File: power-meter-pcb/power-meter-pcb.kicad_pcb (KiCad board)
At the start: 4 copper layers, 23 x 51.5 mm, 62 parts, among them J1 Crank interconnect, J2 Debug, J3 Spare GPIO pins, J4 Battery, J5 USB4120-03-C_REVA, J6 Side A, J7 Side B, Q1 AS2302, SW1 EN, SW2 BOOT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

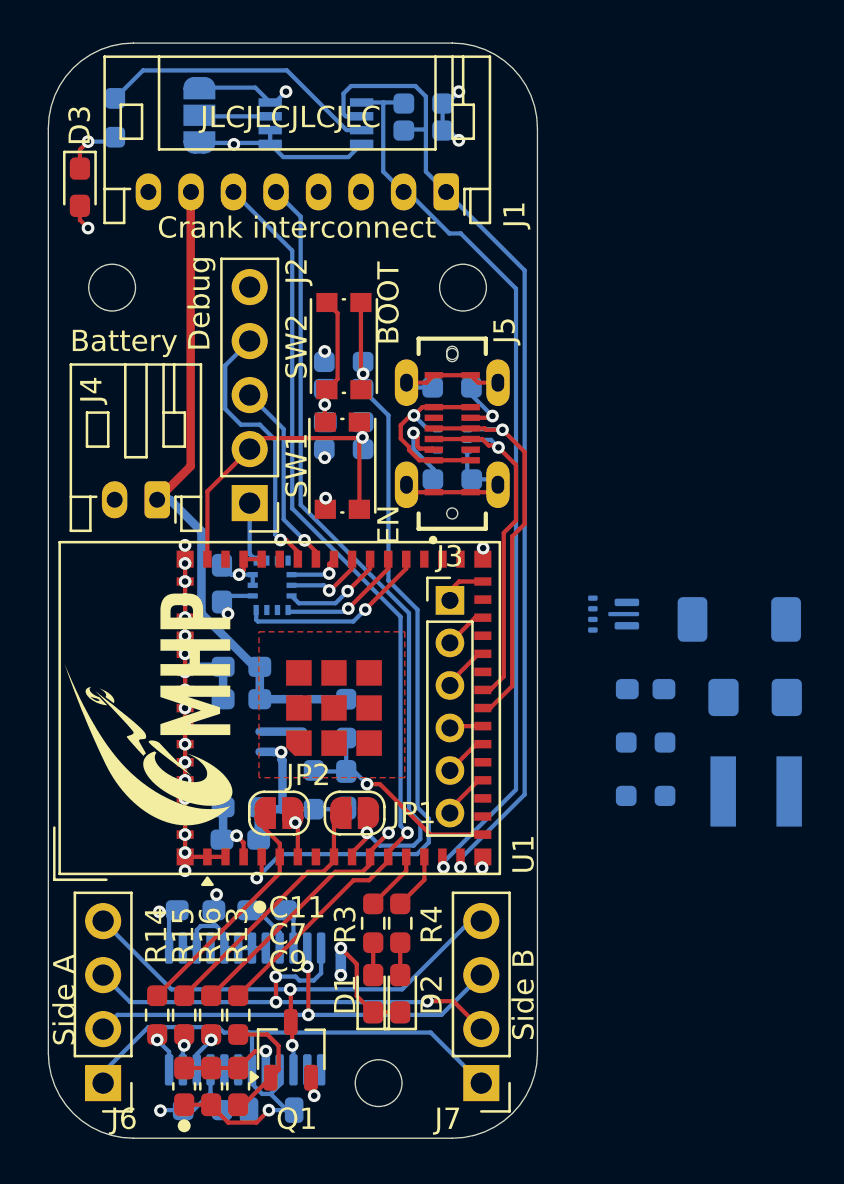
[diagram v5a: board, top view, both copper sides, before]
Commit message: New voltage regulator layout about done
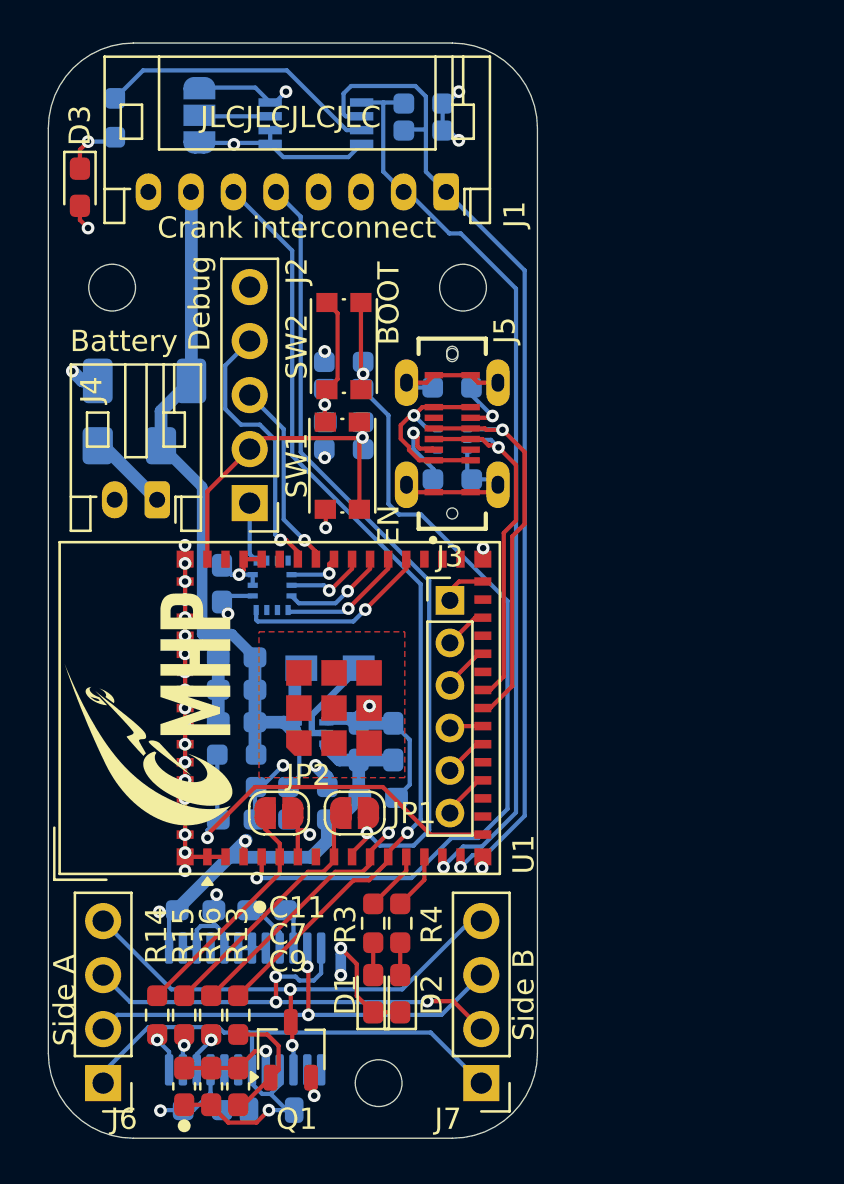
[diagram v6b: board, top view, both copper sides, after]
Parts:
- added C14: 22u, Capacitor_SMD:C_0603_1608Metric_Pad1.08x0.95mm_HandSolder, B.Cu at (152.8, 96.0)
- L1: value 1u -> 470n; footprint Inductor_SMD_Wurth:L_Wurth_WE-LQSH-4020 -> Inductor_SMD:L_Vishay_IHLP-1212
- U3: value TPS61022 -> TPS61023DRLR; footprint Package_DFN_QFN:Texas_RWU0007A_VQFN-7_2x2mm_P0.5mm -> footprints:DRL0006A
- moved F1 31.7 mm to (147.7, 86.1), turned to 0 degrees
- moved D4 30.1 mm to (148.4, 83.0)
- moved L1 20.9 mm to (157.1, 96.5), turned to 0 degrees
- moved R17 16.3 mm to (156.1, 103.6)
- moved R18 15.9 mm to (156.1, 102.1), turned to 0 degrees
- moved U3 15.3 mm to (156.2, 99.6), turned to 0 degrees
- moved C15 13.6 mm to (159.4, 102.6), turned to 0 degrees
- moved C6 7.78 mm to (160.1, 100.0), turned to 90 degrees
- moved C5 7.23 mm to (158.5, 100.0), turned to 90 degrees
- moved R11 5.42 mm to (152.8, 100.6), turned to 180 degrees
- moved C8 5.34 mm to (152.8, 103.6), turned to 0 degrees
- moved R12 3.63 mm to (152.8, 102.1), turned to 0 degrees
- moved C4 1.11 mm to (152.8, 99.1)
- moved C3 1.11 mm to (152.8, 97.5)
- renumbered C14 to C15
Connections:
- U3 pad 1: GNDD -> Net-(U3-FB)
- U3 pad 2: Net-(U3-SW) -> +BATT
- U3 pad 3: +3.3V -> +BATT
- U3 pad 4: Net-(U3-FB) -> GNDD
- U3 pad 5: +BATT -> Net-(U3-SW)
- U3 pad 6: GNDD -> +3.3V
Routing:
- net +3.3V: track 37.2 -> 50.4 mm
- net /Battery voltage: track 10.8 -> 19.1 mm
- net /BOOT: track 38.6 -> 43.5 mm
- net GNDD: track 76.6 -> 81.5 mm, vias 28 -> 31
- net +BATT: track 31.4 -> 35.3 mm
- net Net-(U3-FB): track 0.00 -> 3.86 mm
- net Net-(J4-+): track 0.00 -> 3.85 mm
- net Net-(U3-SW): track 2.04 -> 4.65 mm
- net /AMP2.DOUT: track 49.0 -> 49.7 mm
- net /AMP_PWDN: track 53.4 -> 54.0 mm
- net /I2C.SDA: track 42.9 -> 43.4 mm
- net /Power save: track 44.9 -> 45.4 mm

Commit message: PCB modifications about done
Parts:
- removed D2: LED, LED_SMD:LED_0603_1608Metric_Pad1.05x0.95mm_HandSolder
- added R19: 150, Resistor_SMD:R_0603_1608Metric_Pad0.98x0.95mm_HandSolder, B.Cu at (158.9, 108.3)
- D1: value LED -> CLX6F-FKC-CNP1ST1E1BB7D3D3; footprint LED_SMD:LED_0603_1608Metric_Pad1.05x0.95mm_HandSolder -> RGB_LED_CLX6F-FKC-CNP1ST1E1BB7D3D3:PLCC6_3.4X3.4_CRW-M
- R3, R4: moved to B.Cu
- U3: footprint footprints:DRL0006A -> TPS61023DRLR:DRL0006A
- moved R3 2.30 mm to (161.5, 108.3)
- moved D1 2.05 mm to (159.7, 109.8)
- moved R4 0.36 mm to (160.2, 108.3)
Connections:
- net /LED2 renamed /LEDG
- D1 pad 2: Net-(D1-A) -> GNDD
- J3 pad 3: /GPIO.26 -> /GPIO.18
- J3 pad 4: /GPIO.18 -> /GPIO.17
- J3 pad 5: /GPIO.17 -> /GPIO.16
- R3 pad 1: /LED1 -> /LEDR
- R3 pad 2: Net-(D1-A) -> Net-(D1-Pad4)
- R4 pad 2: Net-(D2-A) -> Net-(D1-Pad5)
- U1 pad 12: /LED1 -> /LEDB
- U1 pad 16: /Battery voltage -> /LEDR
- U1 pad 17: unconnected-(U1-IO13-Pad17) -> /Battery voltage
- U1 pad 20: unconnected-(U1-IO16-Pad20) -> /GPIO.16
- U1 pad 25: unconnected-(U1-IO21-Pad25) -> /Accelerometer/Interrupt
- U1 pad 26: /GPIO.26 -> unconnected-(U1-IO26-Pad26)
- U1 pad 34: /Accelerometer/Interrupt -> unconnected-(U1-IO38-Pad34)
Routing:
- net +3.3V: track 50.4 -> 67.1 mm, vias 10 -> 9
- net GNDD: track 81.5 -> 91.3 mm, vias 31 -> 30
- net /LEDR: track 0.00 -> 6.71 mm, vias 0 -> 1
- net /LEDB: track 0.00 -> 5.59 mm, vias 0 -> 1
- net /Accelerometer/Interrupt: track 9.02 -> 12.6 mm
- net Net-(D1-Pad4): track 0.00 -> 3.29 mm, vias 0 -> 1
- net Net-(D1-Pad5): track 0.00 -> 3.21 mm, vias 0 -> 1
- net Net-(D1-Pad6): track 0.00 -> 3.09 mm, vias 0 -> 1
- net /LED1: track 2.85 -> 0.00 mm
- net /GPIO.26: track 2.25 -> 0.00 mm
- net /GPIO.16: track 0.00 -> 1.71 mm
- net Net-(D2-A): track 1.52 -> 0.00 mm
- net Net-(D1-A): track 1.52 -> 0.00 mm
- net /GPIO.18: track 1.64 -> 2.84 mm
- net /LEDG: track 2.68 -> 2.53 mm, vias 0 -> 1
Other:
- board text added: "J.G. & O.V. 2024"
- board text removed: "J. Gates & O. Varney, 2024"

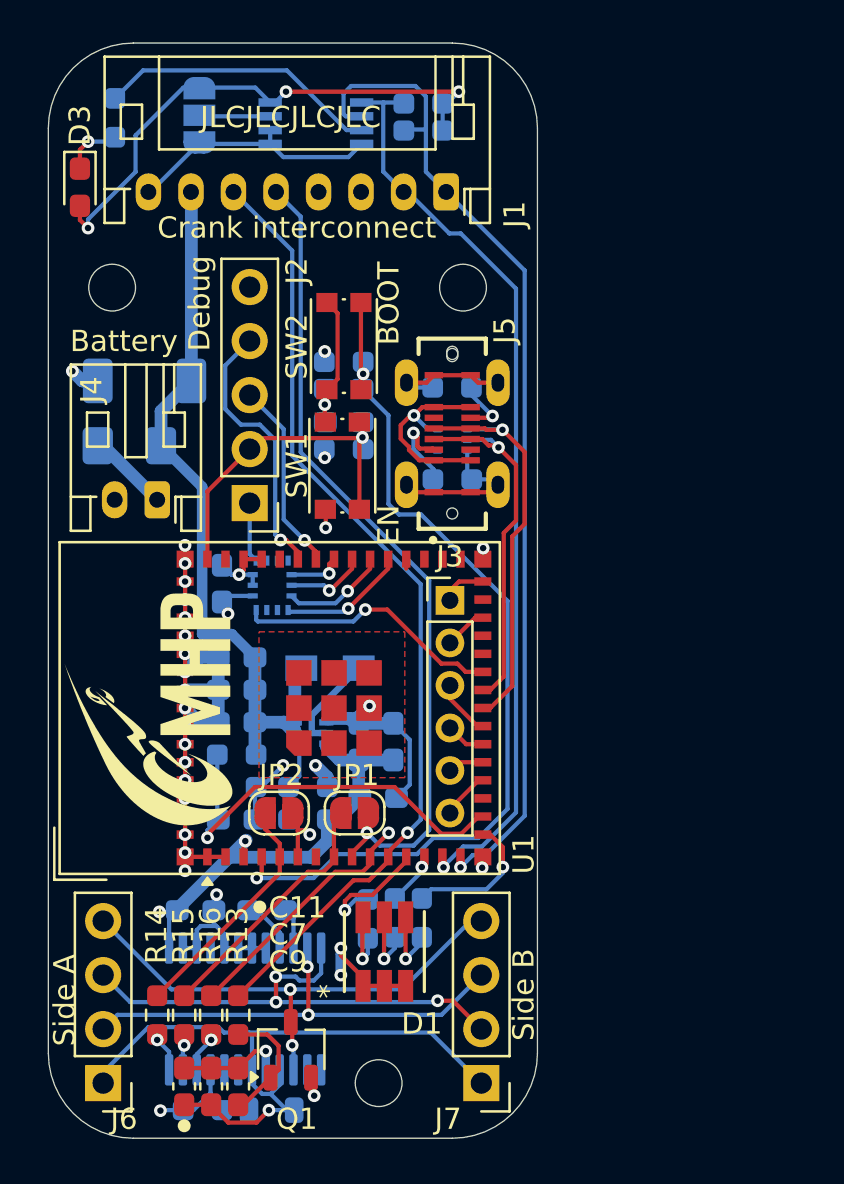
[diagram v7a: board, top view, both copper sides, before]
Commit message: Added slot for thermal isolation
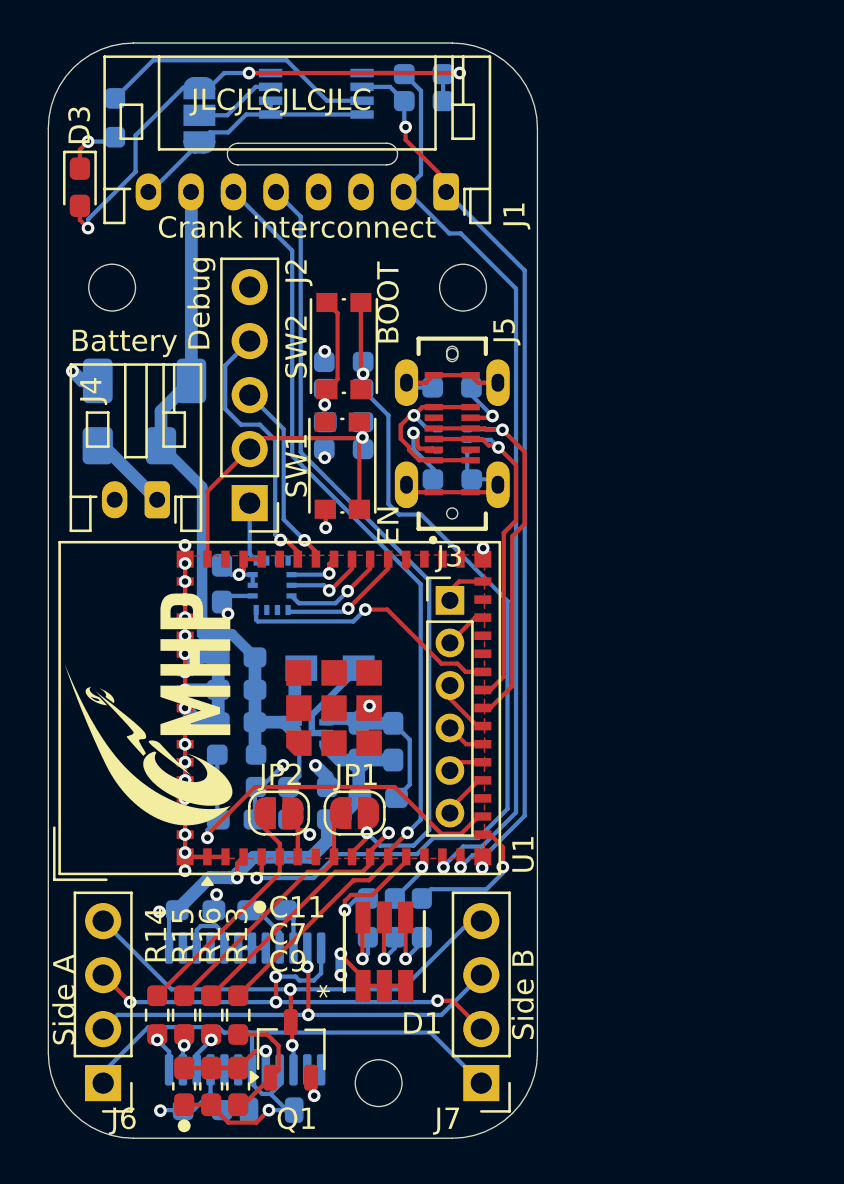
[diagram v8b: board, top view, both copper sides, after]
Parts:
- moved U2 1.38 mm to (156.5, 69.5)
- moved R6 1.38 mm to (161.6, 68.6)
- moved R7 1.38 mm to (161.6, 69.9)
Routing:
- net /I2C.SCL: track 47.4 -> 42.7 mm, vias 1 -> 2
- net /I2C.SDA: track 43.4 -> 45.0 mm
- net GNDD: track 91.3 -> 90.6 mm
- net Net-(JP3-C): track 3.35 -> 3.97 mm
- net +3.3V: track 67.1 -> 67.6 mm
- net /Strain gauge amplifier/GB: vias 3 -> 4
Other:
- outline, holes or cut-outs redrawn
